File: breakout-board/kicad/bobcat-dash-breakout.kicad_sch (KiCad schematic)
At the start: 152 parts, among them J1 TO PI (40-pin ribbon), J10 ADS1115, J11 LIGHTS, J12 COIL, J13 TILT, J14 TEMP PROBE, J2 POWER IN, J3 TO 5V BUCK, J4 SWITCHES, J5 TACH, J6 FUEL, J7 HORN, J8 SILENCE, J9 MAX98357A, Q1 IRLZ44N, Q2 IRF4905, Q3 BC547B, Q4 BC547B, U1 PC817, U10 PC817, U11 DS18B20, U4 PC817, U5 PC817, U6 CD4060BE, U7 PC817, U8 PC817, U9 PC817

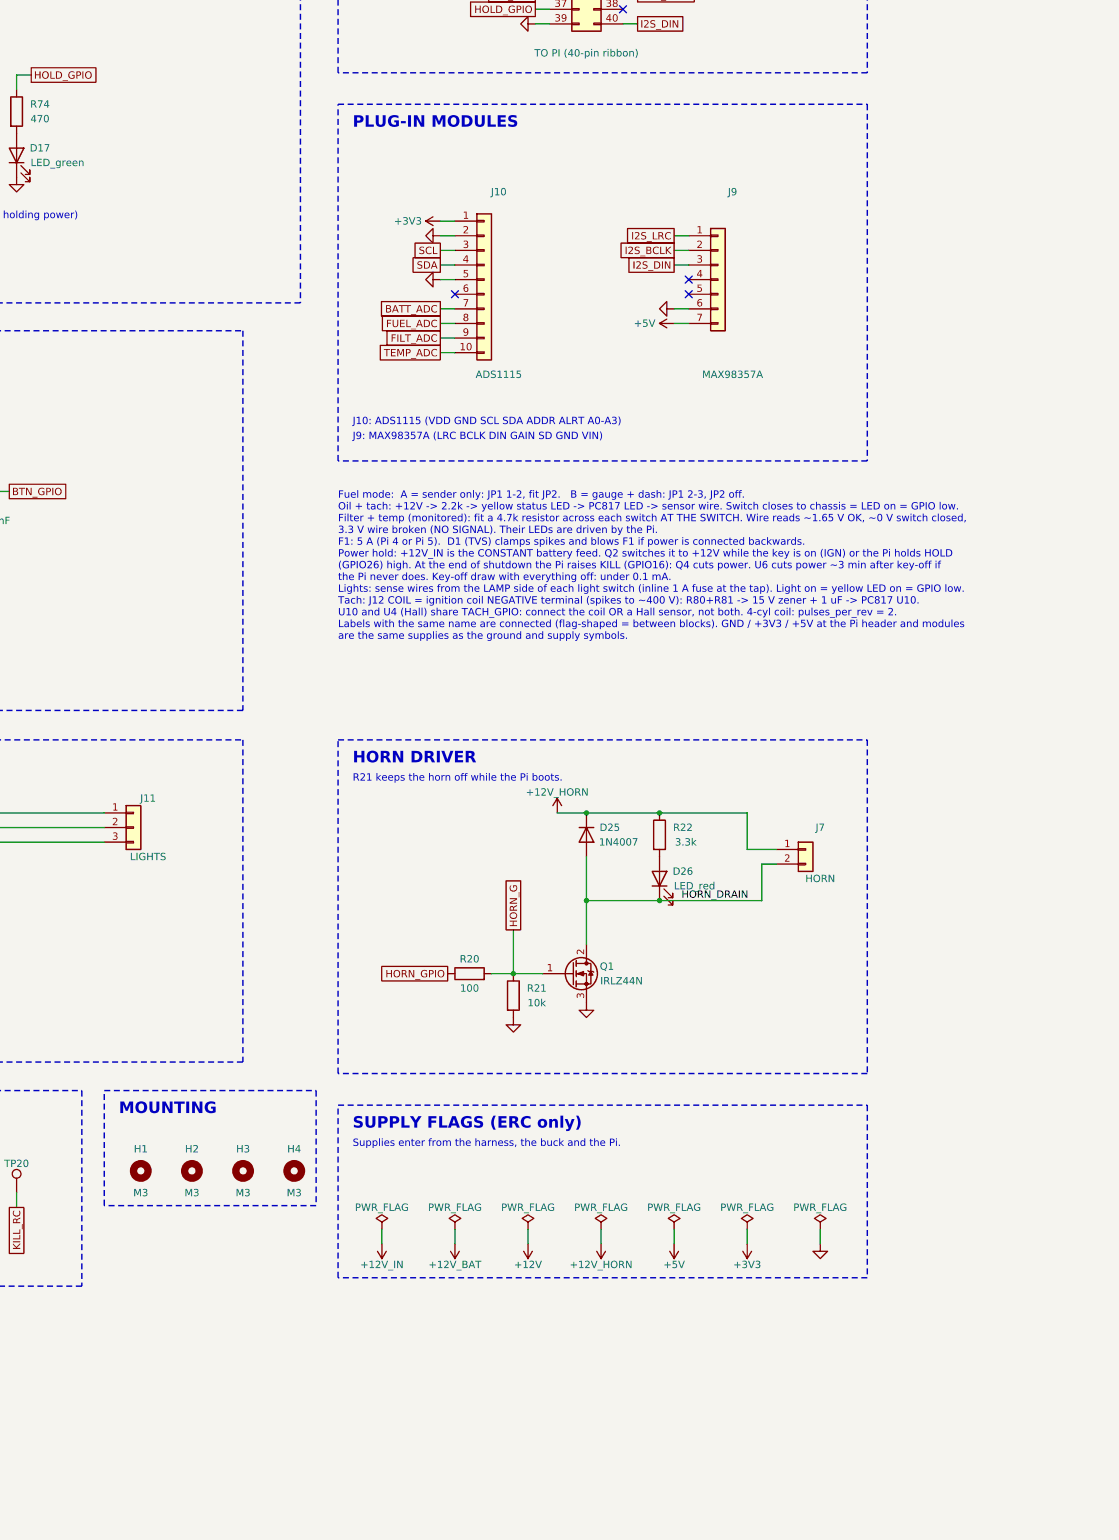
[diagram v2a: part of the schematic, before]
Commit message: Board rev 2.8: two-row ADS1115, mono/stereo amp sites, 162 x 159 mm; ADS1115 adapter
Breakout board rev 2.8:
- ADS1115 (Adafruit 1085, STEMMA QT) plugs straight in: J10 + J15, two 6-pin
  rows 12.7 mm apart, with M2.5 standoff holes H5-H8
- Amp: mono board (Adafruit 3006) on J9 with standoff holes H9-H10, or the
  stereo board (Adafruit 6513) on new J16 with corner holes H11-H14. Same
  I2S signals, fit one only
- Board 25 mm taller (162 x 159 mm): new top strip for the stereo site, the
  title and the Project Moon Pi logo (now on top). Top mounting holes moved:
  153 x 137.5 mm; drilling template updated
- Freerouting output logged to out/route.log (headless: its GUI mode never
  saves the result)

New ADS1115 adapter board (breakout-board/adapter): lets a 10-pin inline
ADS1115 (older Adafruit / clones) plug into the two-row socket, straight-
through wiring, same standoffs, logo top and back. Own generator and build.

Co-Authored-By: Claude Opus 5.5 <noreply@anthropic.com>
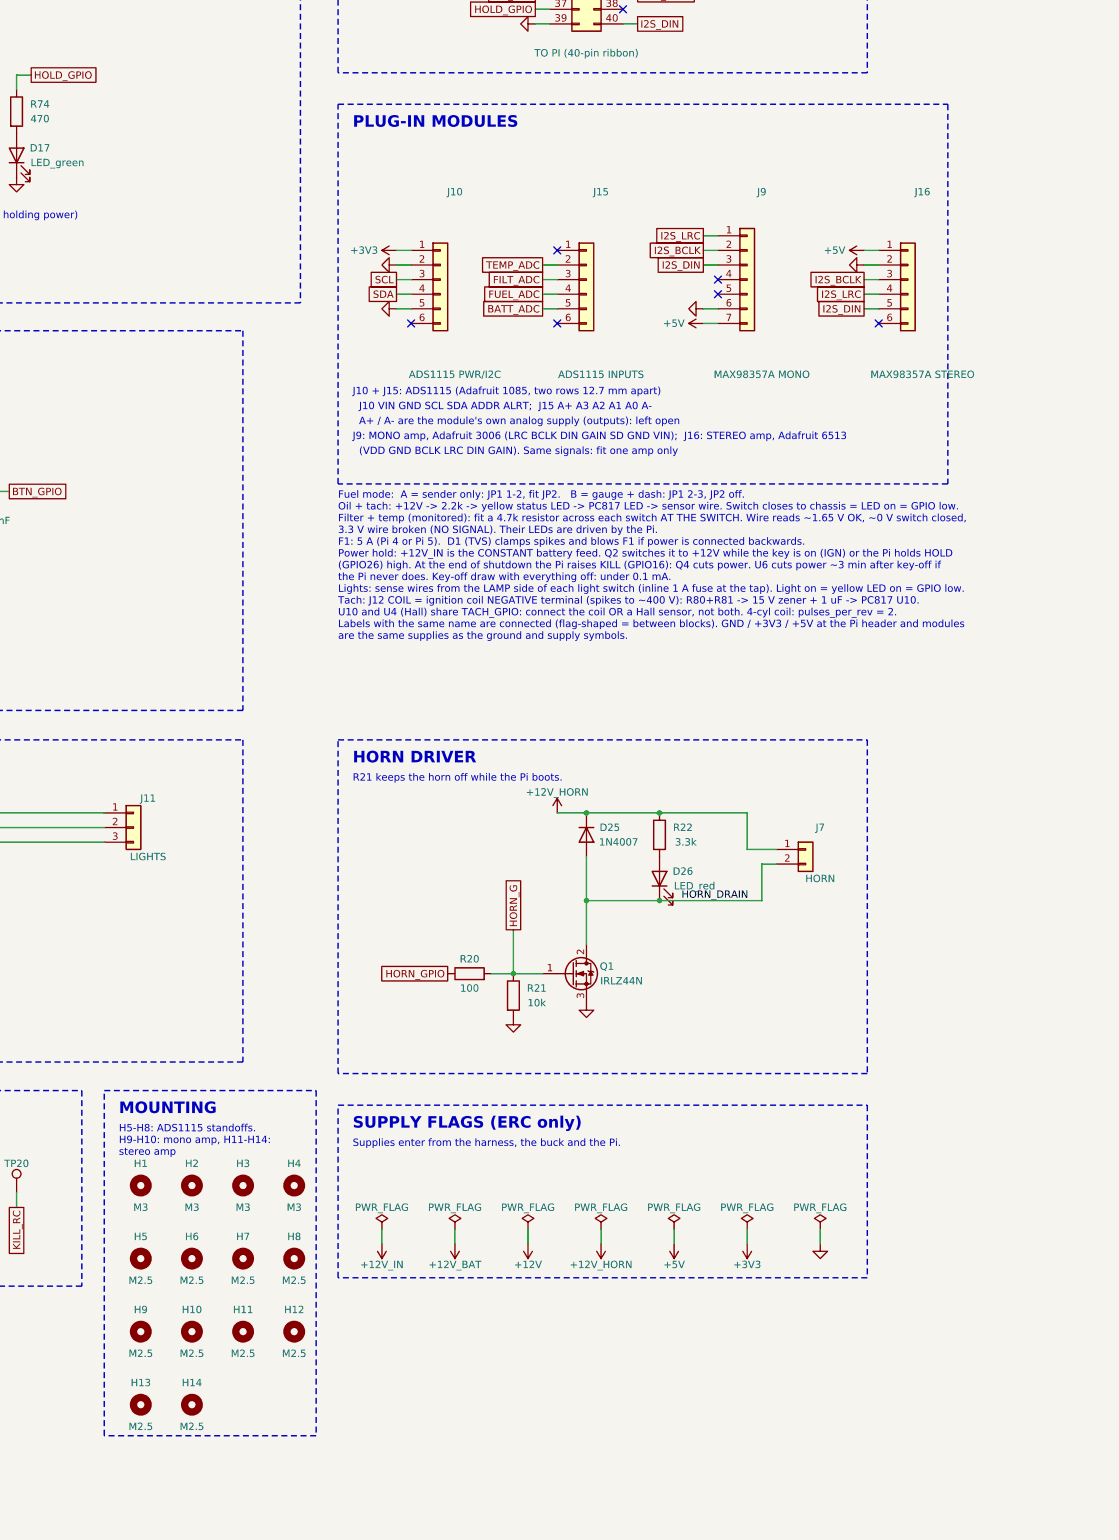
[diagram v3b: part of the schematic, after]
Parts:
- removed J10: ADS1115, Connector_PinSocket_2.54mm:PinSocket_1x10_P2.54mm_Vertical, symbol Connector_Generic:Conn_01x10
- added H10, H11, H12, H13, H14, H5, H6, H7, H8, H9: M2.5, MountingHole:MountingHole_2.7mm_M2.5, symbol Mechanical:MountingHole
- added J10: ADS1115 PWR/I2C, Connector_PinSocket_2.54mm:PinSocket_1x06_P2.54mm_Vertical, symbol Connector_Generic:Conn_01x06
- added J15: ADS1115 INPUTS, Connector_PinSocket_2.54mm:PinSocket_1x06_P2.54mm_Vertical, symbol Connector_Generic:Conn_01x06
- added J16: MAX98357A STEREO, Connector_PinSocket_2.54mm:PinSocket_1x06_P2.54mm_Vertical, symbol Connector_Generic:Conn_01x06
- J9: value MAX98357A -> MAX98357A MONO
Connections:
- net +3V3: now also J10.1 (Pin_1)
- net +5V: now also J16.1 (Pin_1)
- net BATT_ADC: now also J15.5 (Pin_5)
- net FILT_ADC: now also J15.3 (Pin_3)
- net FUEL_ADC: now also J15.4 (Pin_4)
- net GND: now also J10.2 (Pin_2), J10.5 (Pin_5), J16.2 (Pin_2)
- net I2S_BCLK: now also J16.3 (Pin_3)
- net I2S_DIN: now also J16.5 (Pin_5)
- net I2S_LRC: now also J16.4 (Pin_4)
- net SCL: now also J10.3 (Pin_3)
- net SDA: now also J10.4 (Pin_4)
- net TEMP_ADC: now also J15.2 (Pin_2)
- no-connect marks 22 -> 25
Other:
- note added: "(VDD GND BCLK LRC DIN GAIN). Same signals: fit one amp only"
- note added: "A+ / A- are the module's own analog supply (outputs): left open"
- note added: "H5-H8: ADS1115 standoffs. H9-H10: mono amp, H11-H14: stereo amp"
- note added: "J10 + J15: ADS1115 (Adafruit 1085, two rows 12.7 mm apart)"
- note added: "J10 VIN GND SCL SDA ADDR ALRT; J15 A+ A3 A2 A1 A0 A-"
- note added: "J9: MONO amp, Adafruit 3006 (LRC BCLK DIN GAIN SD GND VIN); J16: STEREO amp, Adafruit 6513"
- note removed: "J10: ADS1115 (VDD GND SCL SDA ADDR ALRT A0-A3)"
- note removed: "J9: MAX98357A (LRC BCLK DIN GAIN SD GND VIN)"

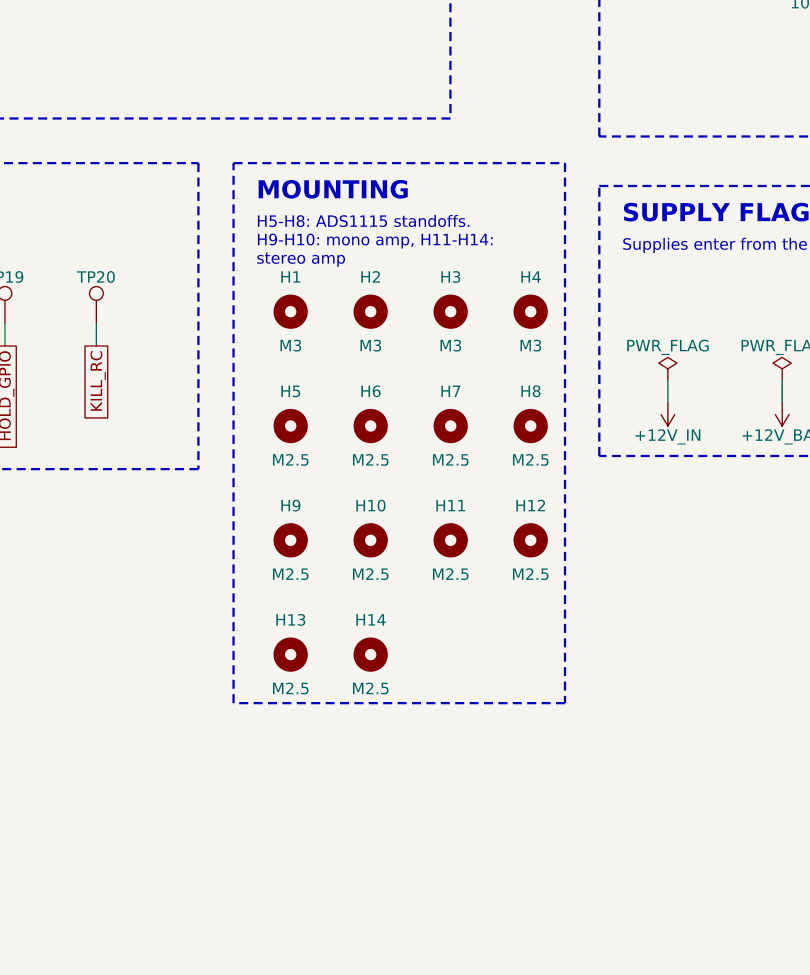
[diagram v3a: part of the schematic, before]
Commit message: Board rev 2.8 re-layout: ribbon header on the top edge, amps side by side, 9 mounting holes, standoff keepouts
- Pi ribbon header J1 and the power LEDs move to the top edge (ribbon goes
  straight up to the lid); TILT plug to the top-left corner
- Stereo amp site J16 now sits beside the mono amp J9 ("fit one amp only")
- 9 M3 mounting holes against vibration: corners, mid-sides (H15-H18) and
  one near the centre (H19); drilling template updated
- Copper-free rings around every hole on both sides (M3 r 4 mm, M2.5 r 3 mm,
  extended to nearby edges): brass standoffs need no insulating washers and
  never tie board ground to the box
- ADS1115 adapter: same standoff keepouts
- README, parts list and BOM spreadsheet updated (9 M3 standoffs, brass notes)

Co-Authored-By: Claude Opus 5.5 <noreply@anthropic.com>
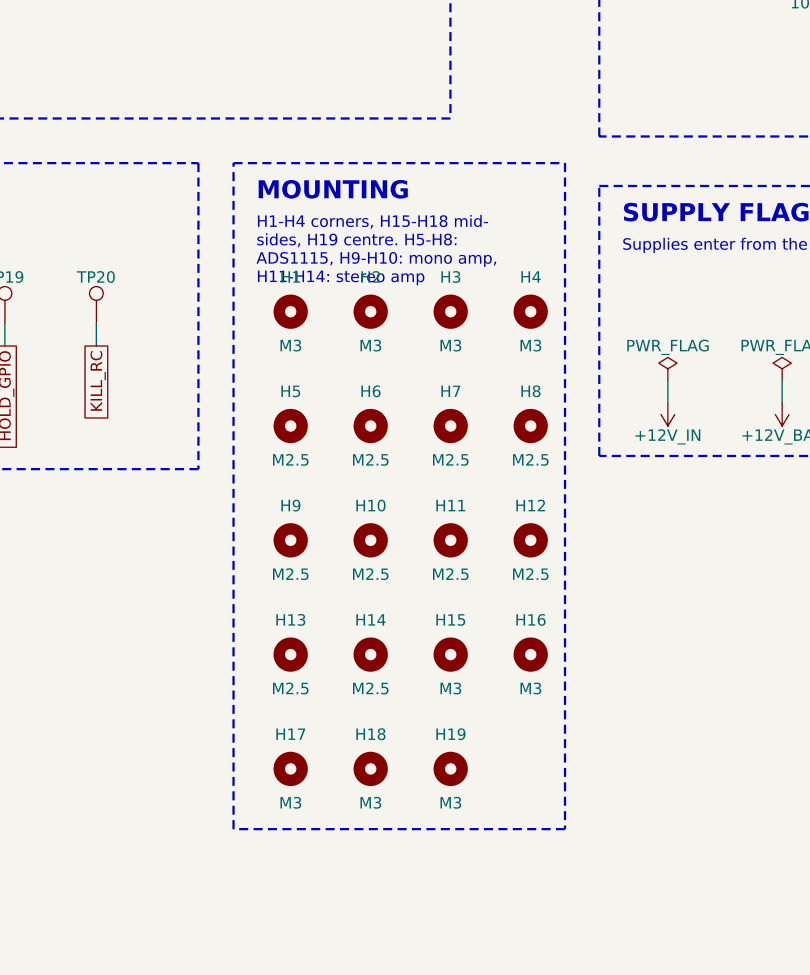
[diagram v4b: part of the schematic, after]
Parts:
- added H15, H16, H17, H18, H19: M3, MountingHole:MountingHole_3.2mm_M3, symbol Mechanical:MountingHole
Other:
- note added: "H1-H4 corners, H15-H18 mid- sides, H19 centre. H5-H8: ADS1115, H9-H10: mono amp, H11-H14: stereo amp"
- note removed: "H5-H8: ADS1115 standoffs. H9-H10: mono amp, H11-H14: stereo amp"

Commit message: S.S.O.M.S: menu screens, service reminders, service Wi-Fi web page, USB stick, board rev 2.9, button pod
Dash (now S.S.O.M.S, System Status, Operations, and Maintenance System; Bobcat M700):
- Menu buttons and screens: HISTORY (clear one / all, ALL ALARMS archive), SERVICE (Bobcat 700 schedule,
  climate setting, details, mark done), SYSTEM; alarms lock the menus until SILENCE; pod fan control.
- Service Wi-Fi (SYSTEM > OK): hotspot + built-in web page (status, performance reports, alarms, service,
  downloads, software update / go back); 30 min countdown, EXTEND on the web page, off at key-off;
  connected devices shown on the dash.
- Usage recording for the reports: full throttle / part throttle / idle / overspeed, starts, hot shutdowns,
  temperatures; day-by-day table paged in the browser (10/20/50/100).
- USB stick: copies the reports and a data backup, offers updates found on the stick.
- Maintenance code (set at first use, no repeated or sequential digits, lockout, recovery code, SD card
  reset-code file): service Wi-Fi, USB install, clearing alarms, marking service done, and the web page's
  install / go back / restart.
- E-BOX (electronics box) temperature naming; S.S.O.M.S splash caption and header.

Breakout board rev 2.9: button pod plug J17 (4 menu buttons, SILENCE, 12 V pod fan via Q5), routed and
DRC clean. route.py shuffles the net order per attempt (Freerouting is deterministic). The generator
also has the next layout change (TILT plug under the E-BOX sensor, new title, edge border), not yet routed.

Button pod enclosure (enclosure/button-pod): Eaton M22 buttons, Pi inside, bolt-on arm and gusset.

Co-Authored-By: Claude Opus 5.5 <noreply@anthropic.com>
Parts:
- added C12, C13, C14, C15: 100nF, Capacitor_THT:C_Disc_D5.0mm_W2.5mm_P5.00mm, symbol Device:C
- added D46: 1N4007, Diode_THT:D_DO-41_SOD81_P10.16mm_Horizontal, symbol Device:D
- added D47: LED_green, LED_THT:LED_D3.0mm, symbol Device:LED
- added J17: POD, Connector_Molex:Molex_Micro-Fit_3.0_43650-0815_1x08_P3.00mm_Vertical, symbol Connector_Generic:Conn_01x08
- added Q5: IRLZ44N, Package_TO_SOT_THT:TO-220-3_Vertical, symbol Transistor_FET:IRLZ44N
- added R89, R90, R91, R92: 1k, Resistor_THT:R_Axial_DIN0207_L6.3mm_D2.5mm_P7.62mm_Horizontal, symbol Device:R
- added R93: 100, Resistor_THT:R_Axial_DIN0207_L6.3mm_D2.5mm_P7.62mm_Horizontal, symbol Device:R
- added R94: 10k, Resistor_THT:R_Axial_DIN0207_L6.3mm_D2.5mm_P7.62mm_Horizontal, symbol Device:R
- added R95: 3.3k, Resistor_THT:R_Axial_DIN0207_L6.3mm_D2.5mm_P7.62mm_Horizontal, symbol Device:R
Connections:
- net +12V: now also D46.1 (K), J17.7 (Pin_7), R95.1
- net GND: now also C12.2, C13.2, C14.2, C15.2, J17.6 (Pin_6), Q5.3 (S), R94.2
- net BTN_IN: now reaches J8.1 (Pin_1), R40.1
- net BTN_IN: now also J17.5 (Pin_5)
- net BTN_BACK_GPIO: now reaches J1.19 (Pin_19)
- net BTN_BACK_GPIO: now also C15.1, R92.2
- net FAN_GPIO: now reaches J1.23 (Pin_23)
- net FAN_GPIO: now also R93.1
- net BTN_L_GPIO: now reaches J1.24 (Pin_24)
- net BTN_L_GPIO: now also C12.1, R89.2
- net BTN_R_GPIO: now reaches J1.26 (Pin_26)
- net BTN_R_GPIO: now also C13.1, R90.2
- net BTN_OK_GPIO: now reaches J1.38 (Pin_38)
- net BTN_OK_GPIO: now also C14.1, R91.2
- new net: Q5.1 (G), R93.2, R94.1
- new net: D47.2 (A), R95.2
- new net BTN_BACK_IN: J17.4 (Pin_4), R92.1
- new net BTN_L_IN: J17.1 (Pin_1), R89.1
- new net BTN_OK_IN: J17.3 (Pin_3), R91.1
- new net BTN_R_IN: J17.2 (Pin_2), R90.1
- new net FAN_DRAIN: D46.2 (A), D47.1 (K), J17.8 (Pin_8), Q5.2 (D)
- no-connect marks 25 -> 20
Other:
- note added: "BUTTON POD (rev 2.9)"
- note added: "J17 to the pod on the box top: 4 menu buttons and ALARM SILENCE to GND, and the pod's 12 V exhaust fan. Buttons filtered like SILENCE (1k + 100 nF). The Pi switches the fan through Q5; R94 keeps it off at boot."
- note added: "J17: 1 LEFT 2 RIGHT 3 OK 4 BACK 5 SILENCE 6 GND 7 FAN +12V 8 FAN -"
- note added: "M3: H1-4 corners, H15-18 sides, H19 centre. M2.5: H5-8 ADC, H9-10 mono, H11-14 stereo amp"
- note removed: "H1-H4 corners, H15-H18 mid- sides, H19 centre. H5-H8: ADS1115, H9-H10: mono amp, H11-H14: stereo amp"

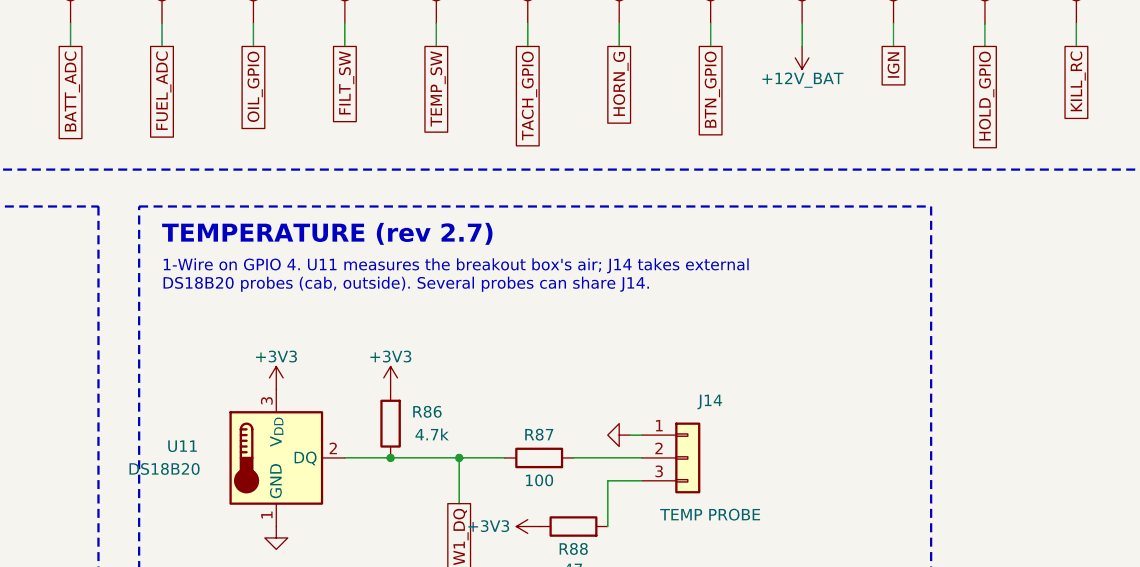
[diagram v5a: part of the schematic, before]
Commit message: M.O.S.S. rename, settings, B612 font, board rev 2.9 layout (blue, 0.6 mm supplies)
Software:
- System renamed M.O.S.S. (Maintenance, Operations, and Service System);
  Wi-Fi SSID and USB folder MOSS-BOBCAT-M700
- Maintenance code: lockout, recovery code, SD-card reset; gates clears,
  mark done, clock, Wi-Fi, USB and web install/restore/restart;
  "are you sure?" pop-ups default to NO
- Settings: C/F units, 12h/24h clock, set clock (device sync / by hand on
  web or dash), named time zone with automatic DST
- Web: status tiles (engine status links to service/alarms), Wi-Fi EXTEND,
  reports with daily temp/battery charts, extremes with time, paged day
  table, throttle bands reframed; alarm durations to the second
- B612 font on the dash and web; BOX renamed E-BOX

Board rev 2.9:
- TILT plug level with the ADC module, TEMP column 7 mm lower, H18 moved
- +3V3 and +5V at 0.6 mm, signals 0.3 mm / 0.25 mm, 0.8 mm edge keepout
- Blue solder mask (main board and ADS1115 adapter); routed, DRC clean
- adapter/ renamed ads1115-adapter/; diagrams and BOM moved to docs/

Co-Authored-By: Claude Opus 5.5 <noreply@anthropic.com>
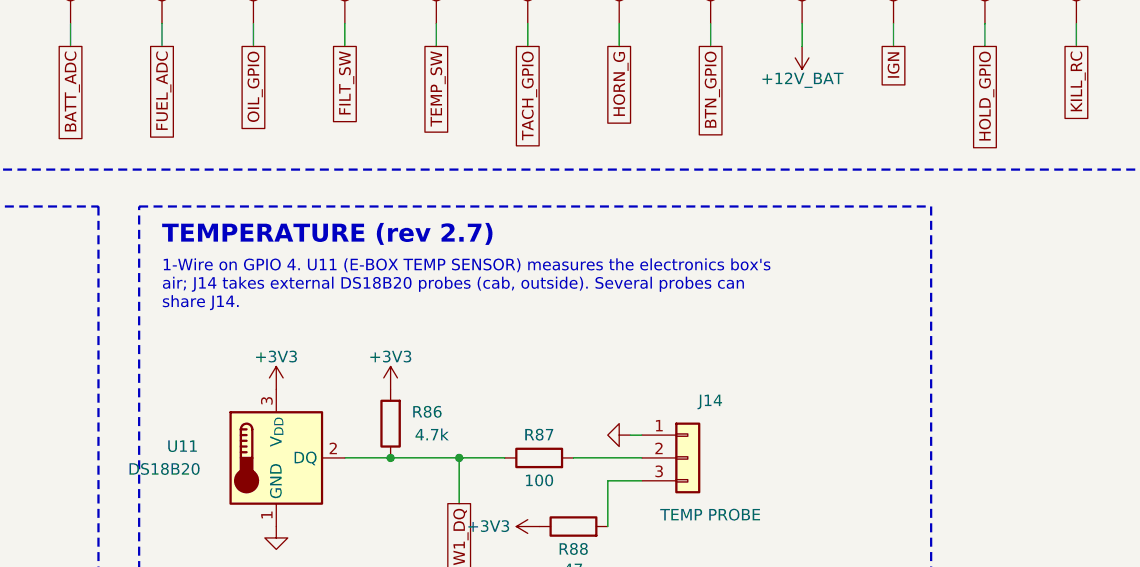
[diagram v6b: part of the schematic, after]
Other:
- note added: "1-Wire on GPIO 4. U11 (E-BOX TEMP SENSOR) measures the electronics box's air; J14 takes external DS18B20 probes (cab, outside). Several probes can share J14."
- note removed: "1-Wire on GPIO 4. U11 measures the breakout box's air; J14 takes external DS18B20 probes (cab, outside). Several probes can share J14."
- title: Bobcat Digital Dash - Breakout Board -> M.O.S.S. Breakout Board - Bobcat M700
